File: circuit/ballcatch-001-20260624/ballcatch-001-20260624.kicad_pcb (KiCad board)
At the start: 2 copper layers, 55.6 x 32.2 mm, 5 parts, among them J1 Conn_01x03_Pin, Q1 Q_Photo_NPN_CE

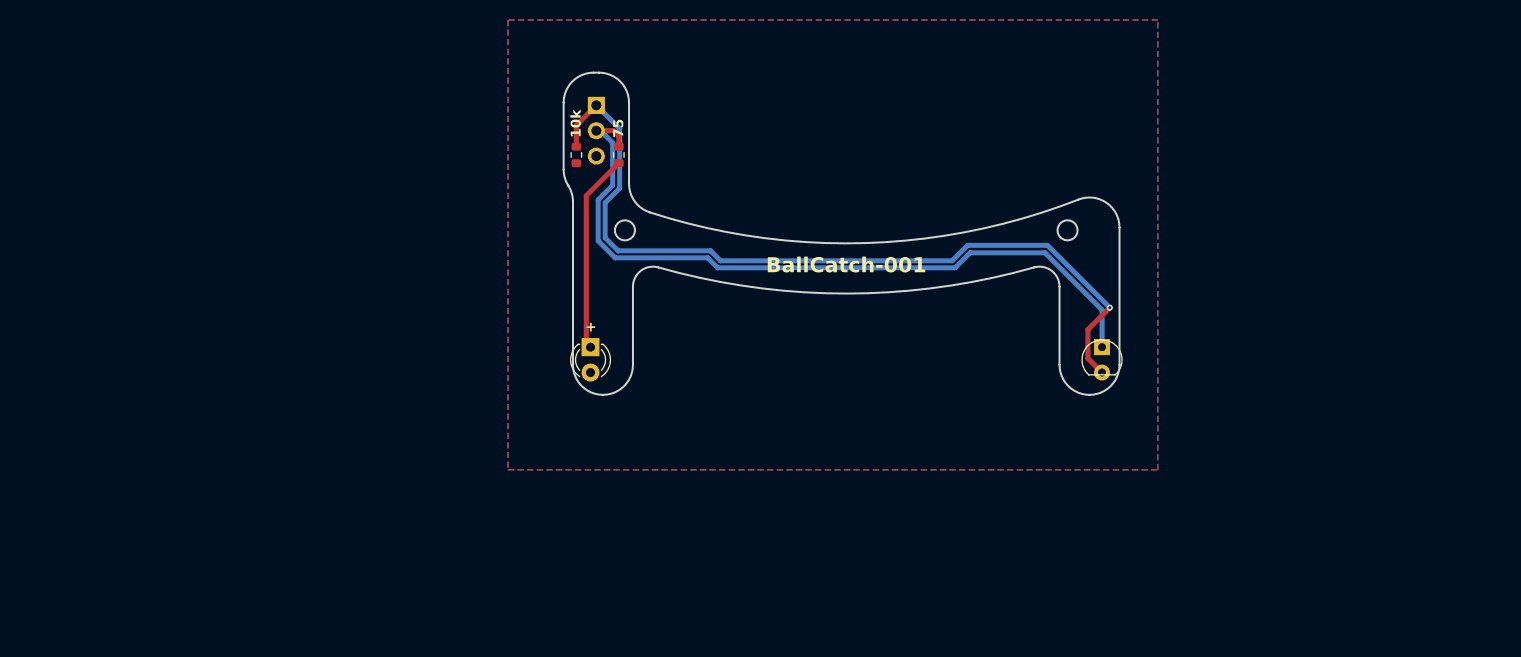
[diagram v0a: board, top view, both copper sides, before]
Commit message: Update ボール補足基板のボード図を完成させた
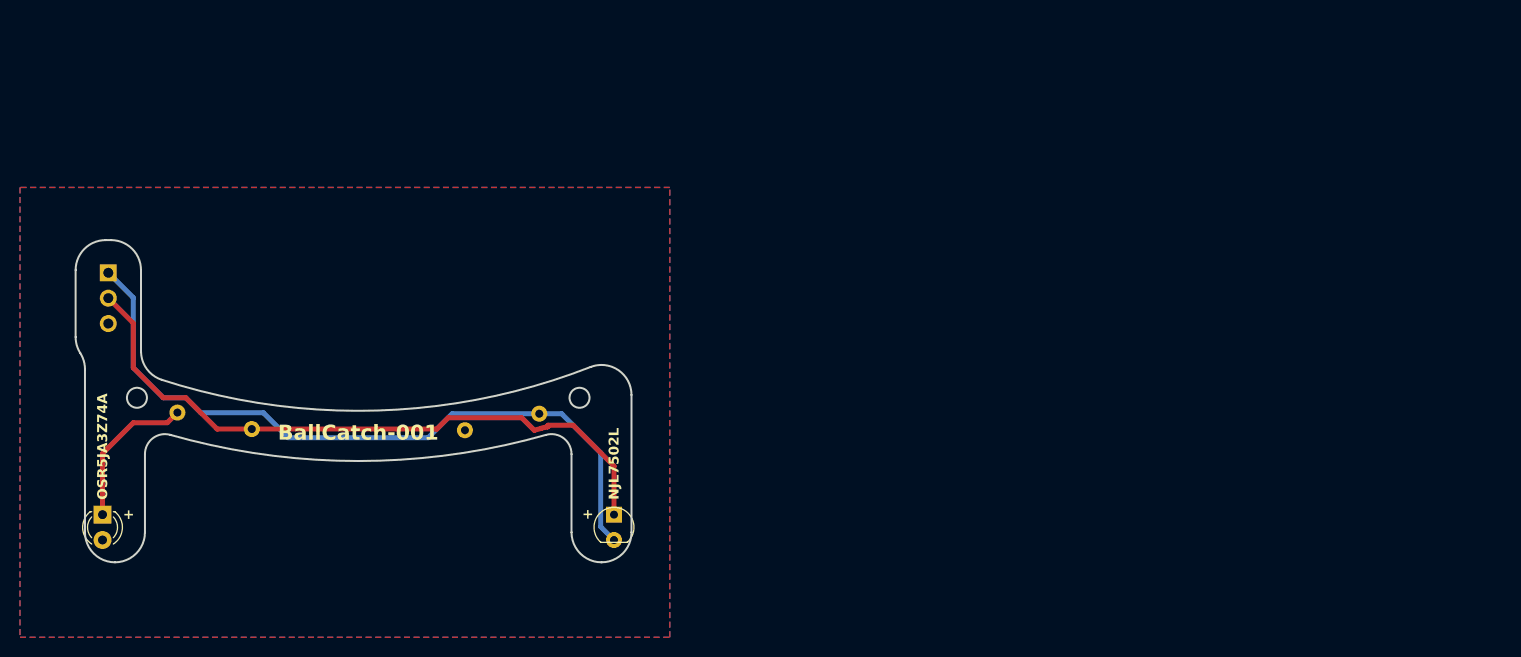
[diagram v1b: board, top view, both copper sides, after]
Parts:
- D1: value LED -> OSR5JA3Z74A
- J1: value Conn_01x03_Pin -> Conn_BallCatch
- Q1: value Q_Photo_NPN_CE -> NJL7502L
- R1, R2: footprint Resistor_SMD:R_0603_1608Metric -> Resistor_THT:R_Axial_DIN0207_L6.3mm_D2.5mm_P7.62mm_Horizontal; moved to B.Cu
- moved Q1 51.6 mm to (26.0, 75.8)
- moved D1 51.6 mm to (-25.2, 74.5)
- moved J1 51.6 mm to (-24.6, 50.3)
- moved R1 45.8 mm to (-10.2, 65.9), turned to 167.5 degrees
- moved R2 26.1 mm to (18.5, 64.4), turned to -167.5 degrees
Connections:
- R1 pad 1: Net-(D1-A) -> +3.3V
- R1 pad 2: +3.3V -> Net-(D1-A)
- R2 pad 1: GND -> BallCatch_{Back}
- R2 pad 2: BallCatch_{Back} -> GND
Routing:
- net BallCatch_{Back}: track 82.4 -> 72.1 mm, vias 1 -> 0
- net +3.3V: track 74.3 -> 66.4 mm
- net Net-(D1-A): track 19.9 -> 15.3 mm

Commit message: Update ボール補足センサの発注ファイルと3Dを出力
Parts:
- moved D1 83.3 mm to (58.0, 70.3)
- moved R1 83.3 mm to (73.0, 61.7)
- moved R2 83.3 mm to (101.7, 60.2)
- moved J1 83.3 mm to (58.6, 46.1)
- moved Q1 83.3 mm to (109.2, 71.5)
